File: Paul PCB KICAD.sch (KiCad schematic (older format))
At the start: 160 parts, among them SW1 SW_Push, U1 ATmega32U4-AU, Y1 16MHz

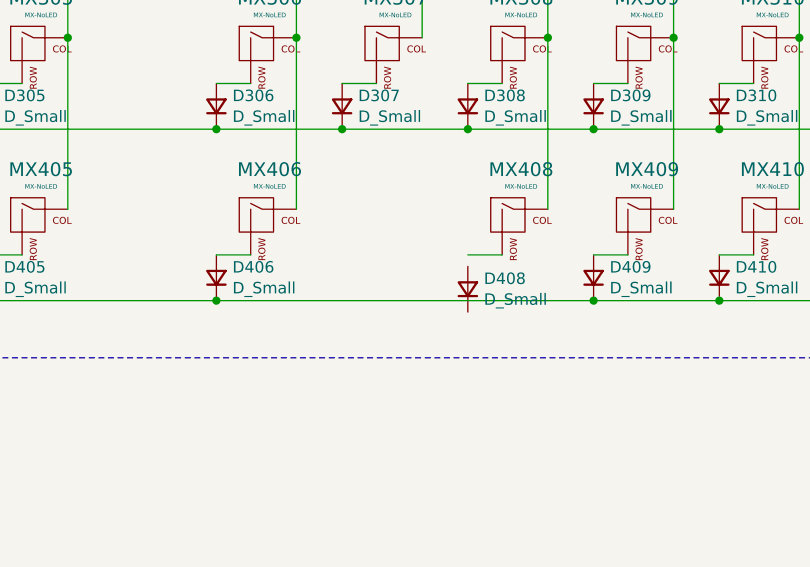
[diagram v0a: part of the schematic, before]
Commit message: Finished Prelim Diode Placement
Beginning to Route Tracks
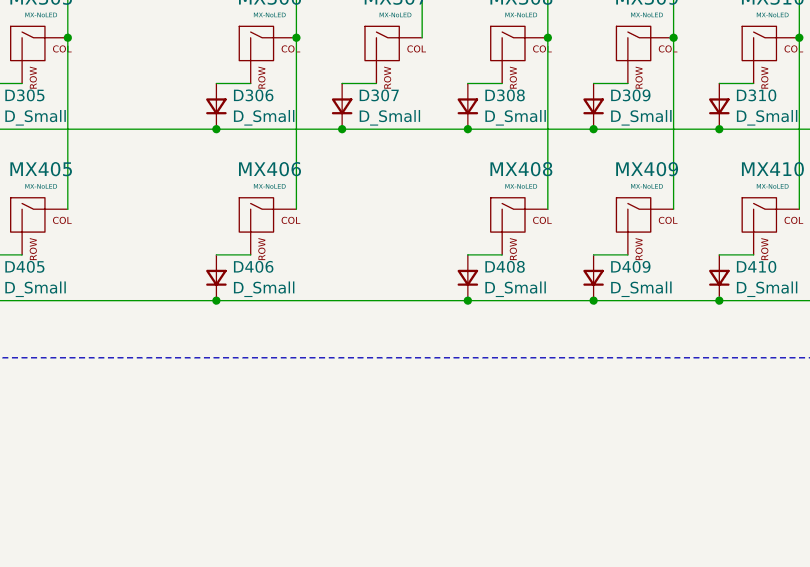
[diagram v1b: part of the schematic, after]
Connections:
- net ROW4: now also D408.1 (K)
- net at MX408.2 (ROW): now also D408.2 (A)
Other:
- moved on the sheet: D408
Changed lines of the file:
@@
 L Device:D_Small D408
 U 1 1 6086EB1E
-P 11600 5150
-F 0 "D408" V 11646 5080 50  0000 R CNN
-F 1 "D_Small" V 11555 5080 50  0000 R CNN
-F 2 "Diode_SMD:D_SOD-123" V 11600 5150 50  0001 C CNN
-F 3 "~" V 11600 5150 50  0001 C CNN
-	1    11600 5150
+P 11600 5100
+F 0 "D408" V 11646 5030 50  0000 R CNN
+F 1 "D_Small" V 11555 5030 50  0000 R CNN
+F 2 "Diode_SMD:D_SOD-123" V 11600 5100 50  0001 C CNN
+F 3 "~" V 11600 5100 50  0001 C CNN
+	1    11600 5100
 	0    -1   -1   0
 $EndComp
@@
 Connection ~ 10500 5200
 Wire Wire Line
-	10500 5200 12150 5200
+	10500 5200 11600 5200
 Wire Wire Line
 	9850 4800 9850 4050
@@
 Wire Wire Line
 	11950 3350 11950 4050
-Connection ~ 11950 4050
-Wire Wire Line
-	11950 4050 11950 4800
 Connection ~ 12150 5200
 Connection ~ 12700 5200
@@
 Text Label 3050 3150 0    50   ~ 0
 USB_N
+Wire Wire Line
+	11950 4050 11950 4800
+Connection ~ 11950 4050
+Connection ~ 11600 5200
+Wire Wire Line
+	11600 5200 12150 5200
 $EndSCHEMATC

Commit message: Finished V1.0
I think it may be done
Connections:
- net Rot.Enc.C is gone; now on net GND: RotaryEncoder1.C
- net COL0: now also U1.36 (PF7)
- net COL1: now also U1.37 (PF6)
- net COL10: now also U1.20 (PD2)
- net COL11: now also U1.21 (PD3)
- net COL12: now also U1.27 (PD7)
- net COL13: now also U1.12 (PB7)
- net COL14: now also U1.28 (PB4)
- net COL2: now also U1.38 (PF5)
- net COL3: now also U1.39 (PF4)
- net COL4: now also U1.40 (PF1)
- net COL5: now also U1.41 (PF0)
- net COL6: now also U1.10 (PB2)
- net COL7: now also U1.11 (PB3)
- net COL8: now also U1.18 (PD0)
- net COL9: now also U1.19 (PD1)
- net ROW0: now also U1.9 (PB1)
- net ROW1: now also U1.8 (PB0)
- net ROW2: now also U1.22 (PD5)
- net ROW3: now also U1.29 (PB5)
- net ROW4: now also U1.30 (PB6)
- net Rot.Enc.A: now also U1.25 (PD4)
- net Rot.Enc.B: now also U1.26 (PD6)
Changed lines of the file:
@@
 	5700 1150 5700 5450
-Wire Notes Line
-	5700 5450 15800 5450
 Wire Notes Line
 	15800 5450 15800 1150
@@
 Text GLabel 14450 6250 2    50   Input ~ 0
 Rot.Enc.A
-Text GLabel 14450 6350 2    50   Input ~ 0
-Rot.Enc.C
 Text GLabel 14450 6450 2    50   Input ~ 0
 Rot.Enc.B
@@
 Wire Wire Line
 	11600 5200 12150 5200
+Text GLabel 5050 4950 2    50   Input ~ 0
+COL0
+Text GLabel 5050 4850 2    50   Input ~ 0
+COL1
+Text GLabel 5050 4750 2    50   Input ~ 0
+COL2
+Text GLabel 5050 4650 2    50   Input ~ 0
+COL3
+Text GLabel 5050 4550 2    50   Input ~ 0
+COL4
+Text GLabel 5050 4450 2    50   Input ~ 0
+COL5
+Text GLabel 5050 2050 2    50   Input ~ 0
+ROW1
+Text GLabel 5050 2150 2    50   Input ~ 0
+ROW0
+Text GLabel 5050 2250 2    50   Input ~ 0
+COL6
+Text GLabel 5050 2350 2    50   Input ~ 0
+COL7
+Text GLabel 5050 3250 2    50   Input ~ 0
+COL8
+Text GLabel 5050 3350 2    50   Input ~ 0
+COL9
+Text GLabel 5050 3450 2    50   Input ~ 0
+COL10
+Text GLabel 5050 3550 2    50   Input ~ 0
+COL11
+Text GLabel 5050 3750 2    50   Input ~ 0
+ROW2
+Text GLabel 5050 3950 2    50   Input ~ 0
+COL12
+Text GLabel 5050 2750 2    50   Input ~ 0
+COL13
+Text GLabel 5050 2450 2    50   Input ~ 0
+COL14
+Text GLabel 5050 2550 2    50   Input ~ 0
+ROW3
+Wire Notes Line
+	5700 5450 15800 5450
+Text GLabel 5050 2650 2    50   Input ~ 0
+ROW4
+Text GLabel 5050 3650 2    50   Input ~ 0
+Rot.Enc.A
+Text GLabel 5050 3850 2    50   Input ~ 0
+Rot.Enc.B
+$Comp
+L power:GND #PWR?
+U 1 1 612905BE
+P 15050 6350
+F 0 "#PWR?" H 15050 6100 50  0001 C CNN
+F 1 "GND" H 15055 6177 50  0000 C CNN
+F 2 "" H 15050 6350 50  0001 C CNN
+F 3 "" H 15050 6350 50  0001 C CNN
+	1    15050 6350
+	1    0    0    -1
+$EndComp
+Wire Wire Line
+	14450 6350 15050 6350
 $EndSCHEMATC

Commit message: Added Ground Fill and Changed Reset Switch
Added Ground Fill and Changed Reset Switch
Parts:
- C1: LCSC (none) -> C53987
- C2, C5, C6: LCSC (none) -> C14663
- C3, C4: LCSC (none) -> C1653
- C7: LCSC (none) -> C15849
- C8: LCSC (none) -> C19702
- D0, D1, D10, D100, D101, D102, D103, D104, D105, D106, D107, D108, D109, D11, D110, D111, D112, D113, D114, D12, D13, D14, D2, D200, D201, D202, D203, D204, D205, D206, D207, D208, D209, D210, D211, D212, D214, D3, D300, D301, D302, D303, D304, D305, D306, D307, D308, D309, D310, D311, D312, D314, D4, D400, D401, D402, D404, D405, D406, D408, D409, D410, D411, D412, D414, D5, D6, D7, D8, D9: LCSC (none) -> C64898
- F1: LCSC (none) -> C315893
- R1: LCSC (none) -> C17514
- R2, R3: LCSC (none) -> C27834
- R4, R5: LCSC (none) -> C17561
- R6, R7: LCSC (none) -> C17414
- RotaryEncoder1: LCSC (none) -> C470736
- SW1: footprint random-keyboard-parts:SKQG-1155865 -> TS-1187A-B-A-B:SW_TS-1187A-B-A-B; symbol Switch:SW_Push -> TS-1187A-B-A-B:TS-1187A-B-A-B; LCSC (none) -> C318884
- U1: LCSC (none) -> C44854
- USB1: LCSC (none) -> C165948
- Y1: LCSC (none) -> C13738
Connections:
- net GND: now also SW1.A, SW1.B; no longer SW1.1
- net Reset: now also SW1.C, SW1.D; no longer SW1.2
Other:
- moved on the sheet: RotaryEncoder1
